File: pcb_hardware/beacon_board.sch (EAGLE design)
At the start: 69 parts, among them IC1-AVR ATMEGA32U4TQFP, J1-ISP AVR_SPI_PRG_6PTH, Q1 PZT2222A, Q2 PZT2222A, Q3 PZT2222A, Q4 PZT2222A, Q5 PZT2222A, Q6 PZT2222A, Q7 PZT2222A, Y1 16MHz

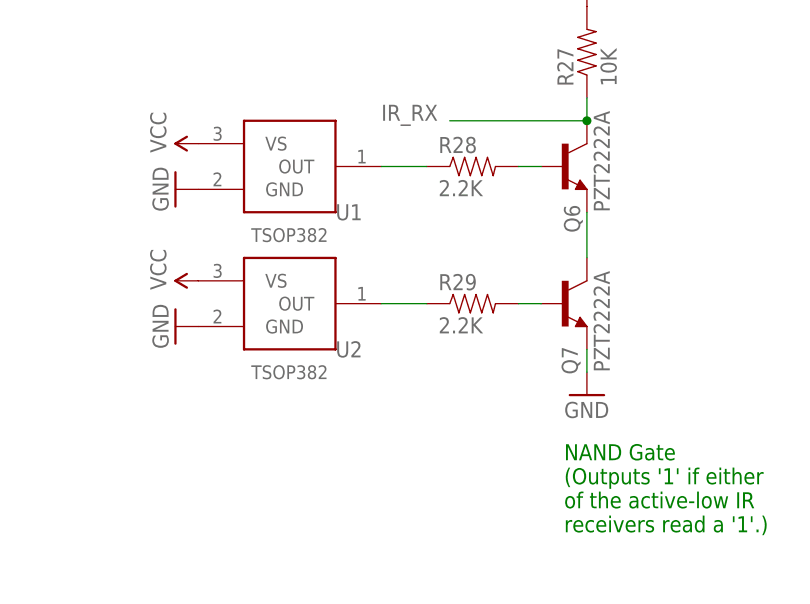
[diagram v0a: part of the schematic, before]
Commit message: Add parallell resistors for TSOP IR receivers
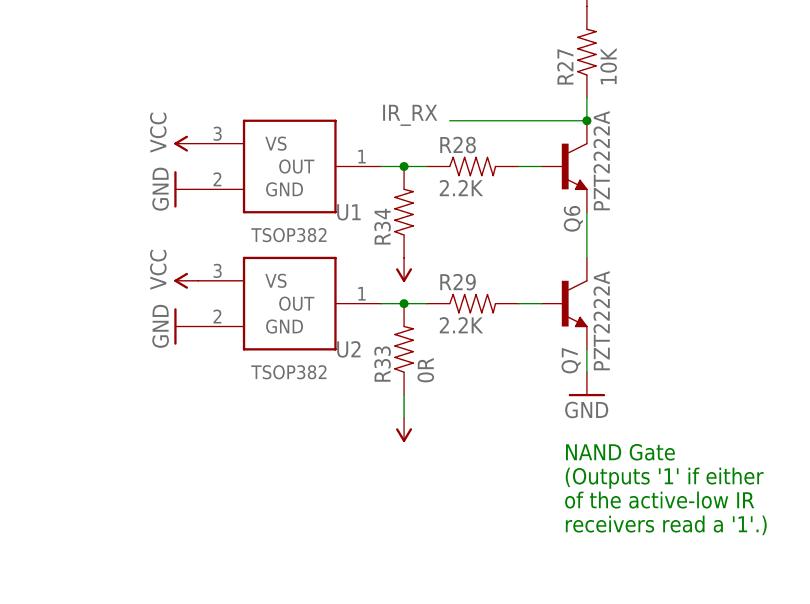
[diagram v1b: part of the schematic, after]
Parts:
- added R33: 0R, SparkFun-Resistors:RESISTOR0805-RES
- added R34: (no value), SparkFun-Resistors:RESISTOR0805-RES
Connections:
- net N$26: now also R34.2
- net N$29: now also R33.2
- net VCC: now also R33.1, R34.1
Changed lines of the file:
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@@
 <part name="R31" library="SparkFun-Passives" deviceset="RESISTOR" device="0805-RES" value="1K"/>
 <part name="R32" library="SparkFun-Passives" deviceset="RESISTOR" device="0805-RES" value="1K"/>
+<part name="SUPPLY12" library="beacon_board" deviceset="VCC" device=""/>
+<part name="R33" library="SparkFun-Resistors" deviceset="RESISTOR" device="0805-RES" value="0R"/>
+<part name="R34" library="SparkFun-Resistors" deviceset="RESISTOR" device="0805-RES"/>
+<part name="P+1" library="SparkFun" deviceset="VCC" device=""/>
 </parts>
 <sheets>
@@
 <instance part="R31" gate="G$1" x="248.92" y="33.02" rot="R90"/>
 <instance part="R32" gate="G$1" x="256.54" y="33.02" rot="R90"/>
+<instance part="SUPPLY12" gate="1" x="213.36" y="139.7" smashed="yes" rot="R180"/>
+<instance part="R33" gate="G$1" x="213.36" y="147.32" rot="R90"/>
+<instance part="R34" gate="G$1" x="213.36" y="162.56" rot="R90"/>
+<instance part="P+1" gate="1" x="213.36" y="157.48" smashed="yes" rot="R180"/>
 </instances>
 <busses>
@@
 <pinref part="SUPPLY11" gate="1" pin="VCC"/>
 </segment>
+<segment>
+<pinref part="SUPPLY12" gate="1" pin="VCC"/>
+<pinref part="R33" gate="G$1" pin="1"/>
+<wire x1="213.36" y1="142.24" x2="213.36" y2="139.7" width="0.1524" layer="91"/>
+</segment>
+<segment>
+<pinref part="R34" gate="G$1" pin="1"/>
+<pinref part="P+1" gate="1" pin="VCC"/>
+</segment>
 </net>
 <net name="N$5" class="0">
@@
 <pinref part="U1" gate="G$1" pin="OUT"/>
 <pinref part="R28" gate="G$1" pin="1"/>
-<wire x1="210.82" y1="167.64" x2="215.9" y2="167.64" width="0.2032" layer="91"/>
+<wire x1="210.82" y1="167.64" x2="213.36" y2="167.64" width="0.2032" layer="91"/>
+<pinref part="R34" gate="G$1" pin="2"/>
+<wire x1="213.36" y1="167.64" x2="215.9" y2="167.64" width="0.2032" layer="91"/>
+<junction x="213.36" y="167.64"/>
 </segment>
 </net>
@@
 <pinref part="U2" gate="G$1" pin="OUT"/>
 <pinref part="R29" gate="G$1" pin="1"/>
-<wire x1="210.82" y1="152.4" x2="215.9" y2="152.4" width="0.2032" layer="91"/>
-</segment>
-</net>
+<wire x1="210.82" y1="152.4" x2="213.36" y2="152.4" width="0.2032" layer="91"/>
+<pinref part="R33" gate="G$1" pin="2"/>
+<wire x1="213.36" y1="152.4" x2="215.9" y2="152.4" width="0.2032" layer="91"/>
+<junction x="213.36" y="152.4"/>
+</segment>
+</net>
